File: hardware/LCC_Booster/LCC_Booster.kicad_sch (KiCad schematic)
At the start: 9 parts, among them J1 A00-216-262-450, J2 Barrel_Jack_MountingPin, J3 Screw_Terminal_01x08, J4 Screw_Terminal_01x02, J5 Screw_Terminal_01x02, SW1 SW_Push, SW2 SW_Slide_DPDT, U1 ACPL-214-500E

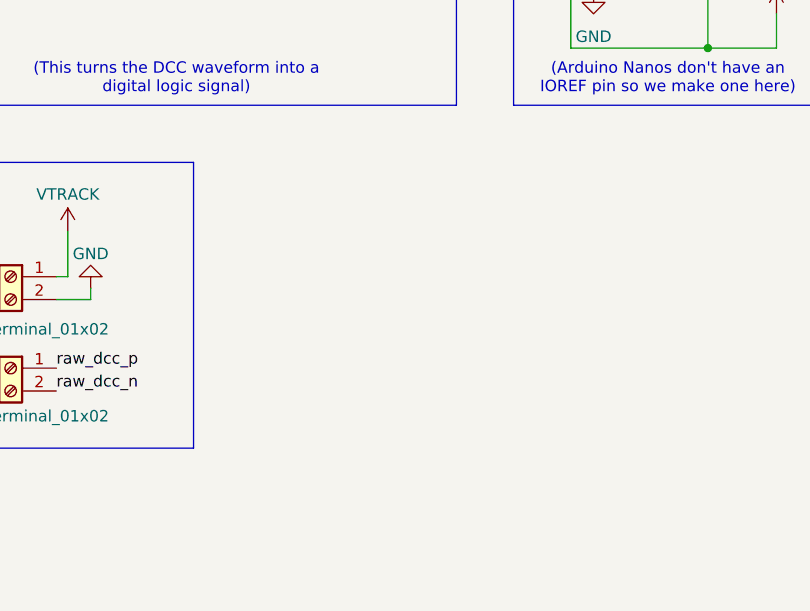
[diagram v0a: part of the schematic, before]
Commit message: Shrunk and added standoffs
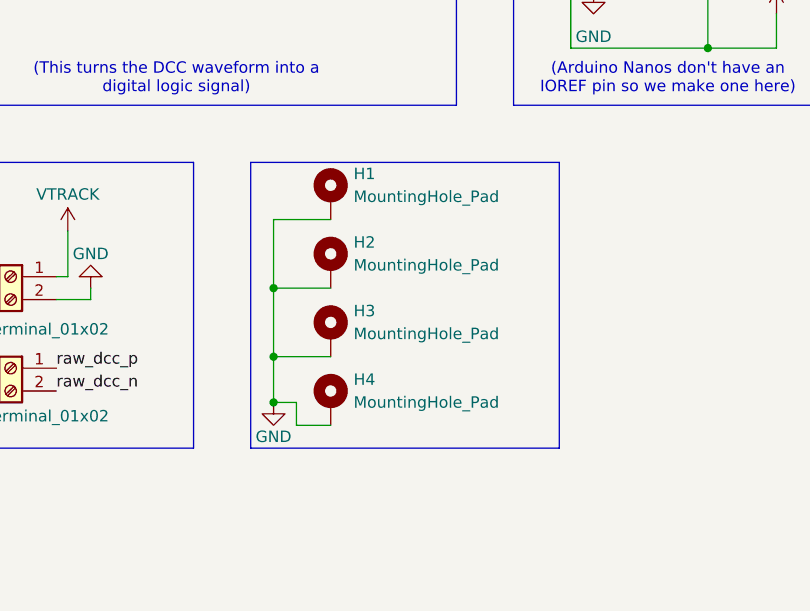
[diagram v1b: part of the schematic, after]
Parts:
- added H1, H2, H3, H4: MountingHole_Pad, MountingHole:MountingHole_4.3mm_M4_Pad_Via, symbol Mechanical:MountingHole_Pad
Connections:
- net GND: now also H1.1, H2.1, H3.1, H4.1

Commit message: Fixed some footprints
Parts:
- removed J2: Barrel_Jack_MountingPin, Connector_BarrelJack:BarrelJack_CUI_PJ-063AH_Horizontal, symbol Connector:Barrel_Jack_MountingPin
- added J2: 54-00166, 54-00166:TENSILITY_54-00166, symbol 54-00166:54-00166
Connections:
- net GND: now also J2.B, J2.C
- net VIN: now also J2.A
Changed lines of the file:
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@@
 	(paper "A4")
 	(junction
+		(at 99.06 137.16)
+		(diameter 0)
+		(color 0 0 0 0)
+	)
+	(junction
 		(at 198.12 66.04)
 		(diameter 0)
@@
 	)
 	(junction
-		(at 93.98 143.51)
-		(diameter 0)
-		(color 0 0 0 0)
-	)
-	(junction
 		(at 198.12 73.66)
 		(diameter 0)
@@
 	(wire
 		(pts
+			(xy 99.06 134.62) (xy 99.06 137.16)
+		)
+		(stroke
+			(width 0)
+			(type default)
+		)
+	)
+	(wire
+		(pts
 			(xy 125.73 19.05) (xy 125.73 48.26)
 		)
@@
 	(wire
 		(pts
-			(xy 93.98 143.51) (xy 90.17 143.51)
-		)
-		(stroke
-			(width 0)
-			(type default)
-		)
-	)
-	(wire
-		(pts
 			(xy 83.82 48.26) (xy 85.09 48.26)
 		)
@@
 	(wire
 		(pts
+			(xy 97.79 134.62) (xy 99.06 134.62)
+		)
+		(stroke
+			(width 0)
+			(type default)
+		)
+	)
+	(wire
+		(pts
 			(xy 93.98 144.78) (xy 93.98 143.51)
 		)
@@
 	(wire
 		(pts
-			(xy 90.17 143.51) (xy 90.17 142.24)
-		)
-		(stroke
-			(width 0)
-			(type default)
-		)
-	)
-	(wire
-		(pts
 			(xy 45.72 20.32) (xy 43.18 20.32)
 		)
@@
 	)
 	(symbol
+		(lib_id "54-00166:54-00166")
+		(at 92.71 134.62 0)
+		(unit 1)
+		(exclude_from_sim no)
+		(in_bom yes)
+		(on_board yes)
+		(dnp no)
+		(fields_autoplaced yes)
+		(property "Reference" "J2"
+			(at 87.9503 125.73 0)
+			(effects
+				(font
+					(size 1.27 1.27)
+				)
+			)
+		)
+		(property "Value" "54-00166"
+			(at 87.9503 128.27 0)
+			(effects
+				(font
+					(size 1.27 1.27)
+				)
+			)
+		)
+		(property "Footprint" "54-00166:TENSILITY_54-00166"
+			(at 92.71 134.62 0)
+			(effects
+				(font
+					(size 1.27 1.27)
+				)
+				(justify bottom)
+				(hide yes)
+			)
+		)
+		(property "Datasheet" ""
+			(at 92.71 134.62 0)
+			(effects
+				(font
+					(size 1.27 1.27)
+				)
+				(hide yes)
+			)
+		)
+		(property "Description" ""
+			(at 92.71 134.62 0)
+			(effects
+				(font
+					(size 1.27 1.27)
+				)
+				(hide yes)
+			)
+		)
+		(property "PARTREV" "A"
+			(at 92.71 134.62 0)
+			(effects
+				(font
+					(size 1.27 1.27)
+				)
+				(justify bottom)
+				(hide yes)
+			)
+		)
+		(property "STANDARD" "Manufacturer Recommendations"
+			(at 92.71 134.62 0)
+			(effects
+				(font
+					(size 1.27 1.27)
+				)
+				(justify bottom)
+				(hide yes)
+			)
+		)
+		(property "SNAPEDA_PN" "54-00166"
+			(at 92.71 134.62 0)
+			(effects
+				(font
+					(size 1.27 1.27)
+				)
+				(justify bottom)
+				(hide yes)
+			)
+		)
+		(property "MAXIMUM_PACKAGE_HEIGHT" "11.2mm"
+			(at 92.71 134.62 0)
+			(effects
+				(font
+					(size 1.27 1.27)
+				)
+				(justify bottom)
+				(hide yes)
+			)
+		)
+		(property "MANUFACTURER" "TENSILITY"
+			(at 92.71 134.62 0)
+			(effects
+				(font
+					(size 1.27 1.27)
+				)
+				(justify bottom)
+				(hide yes)
+			)
+		)
+		(pin "C"
+		)
+		(pin "B"
+		)
+		(pin "A"
+		)
+		(instances
+			(project "LCC_Booster"
+				(path "/e8524381-bb01-4107-93ec-8133e878a3da"
+					(reference "J2")
+					(unit 1)
+				)
+			)
+		)
+	)
+	(symbol
 		(lib_id "Connector:Screw_Terminal_01x02")
 		(at 168.91 74.93 0)
@@
 					(unit 1)
 				)
-			)
-		)
-	)
-	(symbol
-		(lib_id "Connector:Barrel_Jack_MountingPin")
-		(at 90.17 134.62 0)
-		(unit 1)
-		(exclude_from_sim no)
-		(in_bom yes)
-		(on_board yes)
-		(dnp no)
-		(property "Reference" "J2"
-			(at 90.17 129.032 0)
-			(effects
-				(font
-					(size 1.27 1.27)
-				)
-			)
-		)
-		(property "Value" "Barrel_Jack_MountingPin"
-			(at 83.312 139.954 90)
-			(effects
-				(font
-					(size 1.27 1.27)
-				)
-			)
-		)
-		(property "Footprint" "Connector_BarrelJack:BarrelJack_CUI_PJ-063AH_Horizontal"
-			(at 91.44 135.636 0)
-			(effects
-				(font
-					(size 1.27 1.27)
-				)
-				(hide yes)
-			)
-		)
-		(property "Datasheet" "~"
-			(at 91.44 135.636 0)
-			(effects
-				(font
-					(size 1.27 1.27)
-				)
-				(hide yes)
-			)
-		)
-		(property "Description" "DC Barrel Jack with a mounting pin"
-			(at 90.17 134.62 0)
-			(effects
-				(font
-					(size 1.27 1.27)
-				)
-				(hide yes)
-			)
-		)
-		(pin "2"
-		)
-		(pin "MP"
-		)
-		(pin "1"
-		)
-		(instances
-			(project "LCC_Booster"
-				(path "/e8524381-bb01-4107-93ec-8133e878a3da"
-					(reference "J2")
-					(unit 1)
-				)

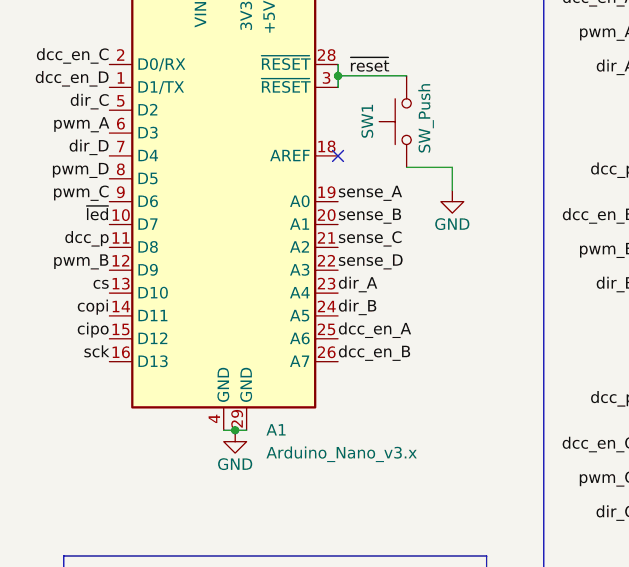
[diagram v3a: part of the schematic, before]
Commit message: LCC Command Station Shield
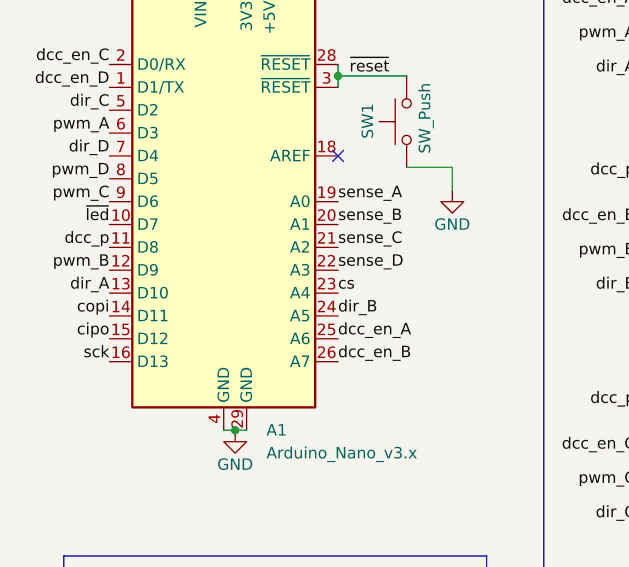
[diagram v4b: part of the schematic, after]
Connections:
- net cs: now also A1.23 (A4); no longer A1.13 (D10)
- net dir_A: now also A1.13 (D10); no longer A1.23 (A4)
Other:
- company: (none) -> TMRC
- title: (none) -> Arduino Nano LCC Booster
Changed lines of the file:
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@@
 	(generator_version "8.0")
 	(paper "A4")
+	(title_block
+		(title "Arduino Nano LCC Booster")
+		(date "2024-04-28")
+		(rev "1.0")
+		(company "TMRC")
+		(comment 1 "Noah Paladino")
+	)
 	(junction
 		(at 99.06 137.16)
@@
 		)
 	)
+	(label "cs"
+		(at 50.8 55.88 0)
+		(fields_autoplaced yes)
+		(effects
+			(font
+				(size 1.27 1.27)
+			)
+			(justify left bottom)
+		)
+	)
 	(label "pwr_n"
 		(at 53.34 124.46 0)
@@
 		)
 	)
-	(label "dir_A"
-		(at 50.8 55.88 0)
-		(fields_autoplaced yes)
-		(effects
-			(font
-				(size 1.27 1.27)
-			)
-			(justify left bottom)
-		)
-	)
 	(label "dcc_p"
 		(at 83.82 68.58 180)
@@
 		)
 	)
+	(label "dir_A"
+		(at 25.4 55.88 180)
+		(fields_autoplaced yes)
+		(effects
+			(font
+				(size 1.27 1.27)
+			)
+			(justify right bottom)
+		)
+	)
 	(label "out1_D"
 		(at 109.22 93.98 0)
@@
 		(fields_autoplaced yes)
 		(effects
-			(font
-				(size 1.27 1.27)
-			)
-			(justify right bottom)
-		)
-	)
-	(label "cs"
-		(at 25.4 55.88 180)
-		(fields_autoplaced yes)
-		(effects

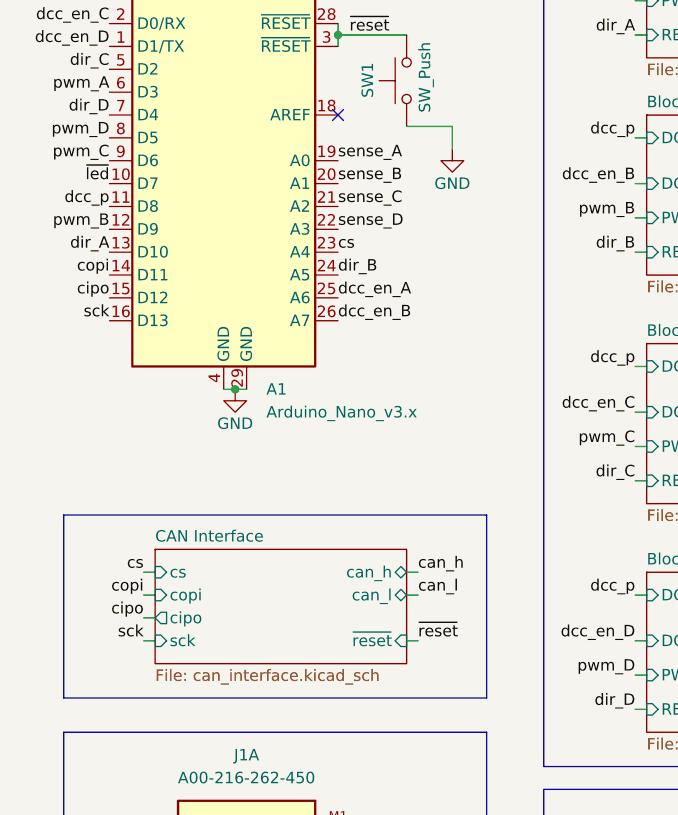
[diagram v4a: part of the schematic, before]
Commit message: Start to work on code structure and added MCP2515 interrupt
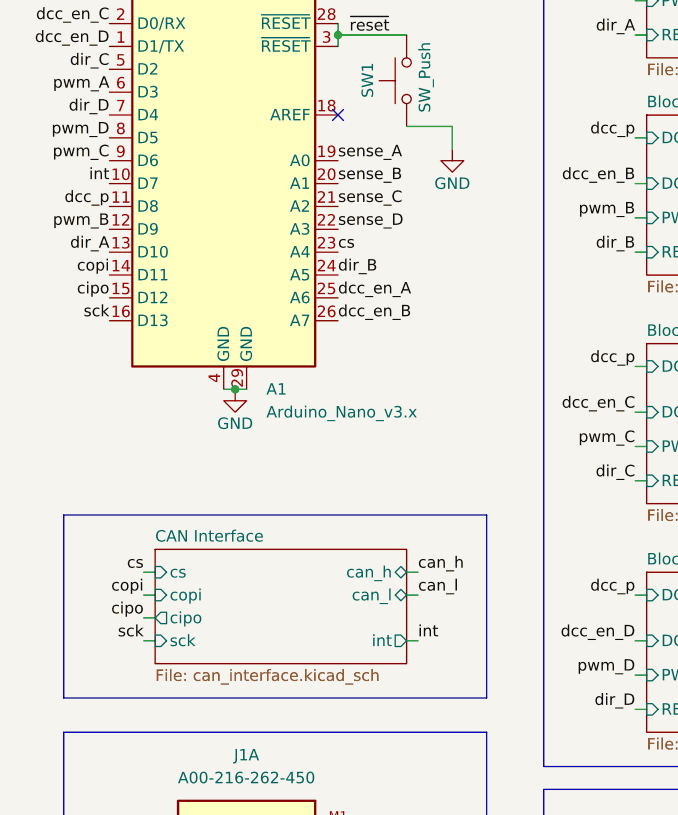
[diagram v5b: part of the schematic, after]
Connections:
- net ~{led} renamed int
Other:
- sheet CAN Interface ports: added int; removed ~{reset}
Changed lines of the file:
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@@
 	(wire
 		(pts
-			(xy 58.42 99.06) (xy 59.69 99.06)
-		)
-		(stroke
-			(width 0)
-			(type default)
-		)
-	)
-	(wire
-		(pts
 			(xy 125.73 48.26) (xy 137.16 48.26)
 		)
@@
 	(wire
 		(pts
+			(xy 58.42 99.06) (xy 59.69 99.06)
+		)
+		(stroke
+			(width 0)
+			(type default)
+		)
+	)
+	(wire
+		(pts
 			(xy 231.14 22.86) (xy 234.95 22.86)
 		)
@@
 		)
 	)
+	(label "int"
+		(at 59.69 99.06 0)
+		(fields_autoplaced yes)
+		(effects
+			(font
+				(size 1.27 1.27)
+			)
+			(justify left bottom)
+		)
+	)
 	(label "out1_A"
 		(at 109.22 19.05 0)
@@
 		)
 	)
-	(label "~{led}"
+	(label "int"
 		(at 25.4 48.26 180)
 		(fields_autoplaced yes)
@@
 		)
 	)
-	(label "~{reset}"
-		(at 59.69 99.06 0)
-		(fields_autoplaced yes)
-		(effects
-			(font
-				(size 1.27 1.27)
-			)
-			(justify left bottom)
-		)
-	)
 	(label "can_gnd"
 		(at 53.34 134.62 0)
@@
 			)
 		)
-		(pin "~{reset}" input
+		(pin "int" output
 			(at 58.42 99.06 0)
 			(effects

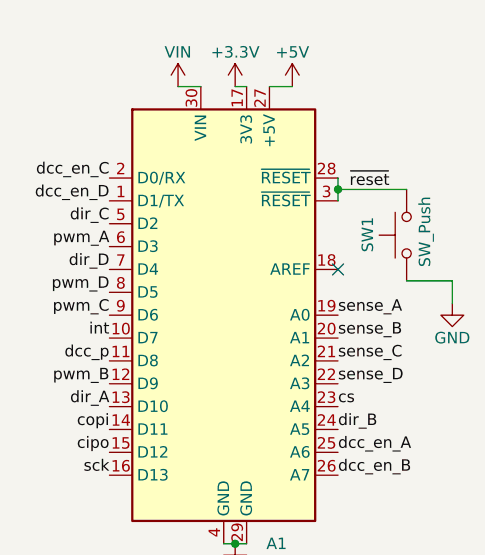
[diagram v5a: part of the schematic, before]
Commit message: Added MCP2515 Interrupt capability
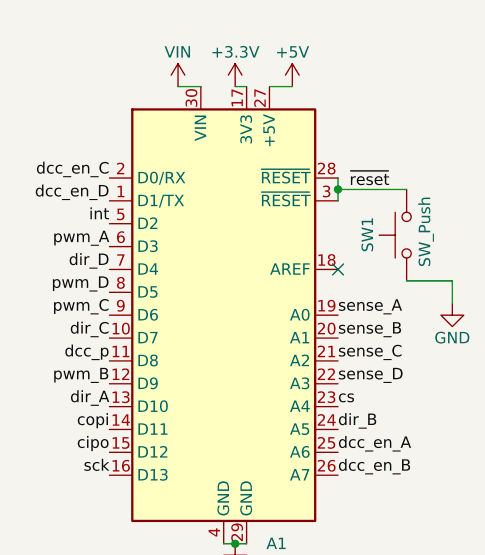
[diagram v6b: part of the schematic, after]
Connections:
- net dir_C: now also A1.10 (D7); no longer A1.5 (D2)
- net int: now also A1.5 (D2); no longer A1.10 (D7)
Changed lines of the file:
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@@
-		)
-	)
-	(label "dir_C"
-		(at 25.4 35.56 180)
-		(fields_autoplaced yes)
-		(effects
-			(font
-				(size 1.27 1.27)
-			)
-			(justify right bottom)
 		)
 	)
@@
 		)
 	)
+	(label "int"
+		(at 25.4 35.56 180)
+		(fields_autoplaced yes)
+		(effects
+			(font
+				(size 1.27 1.27)
+			)
+			(justify right bottom)
+		)
+	)
 	(label "out1_C"
 		(at 109.22 68.58 0)
@@
 		)
 	)
+	(label "dir_C"
+		(at 25.4 48.26 180)
+		(fields_autoplaced yes)
+		(effects
+			(font
+				(size 1.27 1.27)
+			)
+			(justify right bottom)
+		)
+	)
 	(label "dir_B"
 		(at 50.8 58.42 0)
@@
 		)
 	)
-	(label "int"
-		(at 25.4 48.26 180)
-		(fields_autoplaced yes)
-		(effects
-			(font
-				(size 1.27 1.27)
-			)
-			(justify right bottom)
-		)
-	)

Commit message: Better Solder Jumpers, Better Pizza
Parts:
- removed SW2: SW_Slide_DPDT, Button_Switch_THT:SW_CK_JS202011CQN_DPDT_Straight, symbol Switch:SW_Slide_DPDT
- added JP1, JP2: SolderJumper_3_Bridged12, Jumper:SolderJumper-3_P1.3mm_Bridged12_RoundedPad1.0x1.5mm_NumberLabels, symbol Jumper:SolderJumper_3_Bridged12
- added JP5: SolderJumper_2_Open, Jumper:SolderJumper-2_P1.3mm_Open_RoundedPad1.0x1.5mm, symbol Jumper:SolderJumper_2_Open
- J5: now not fitted
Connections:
- net cs is gone; now on net dir_B: A1.23 (A4)
- net +3.3V: now also JP2.1 (A)
- net +5V: now also JP1.1 (A), JP2.3 (B)
- net 3v3_IOREF: now also JP1.2 (C)
- net GND: now also JP1.3 (B), JP5.2 (B)
- net IOREF: now also JP2.2 (C)
- net can_shield: now also JP5.1 (A)
- net dir_A: now also A1.24 (A5); no longer A1.13 (D10)
- net dir_B: no longer A1.24 (A5)
- net int renamed int_cantx
- new net cs_canrx: A1.13 (D10)
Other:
- sheet CAN Interface ports: added cs_canrx, int_cantx; removed cs, int

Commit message: Update to hardware v2 and cleanup
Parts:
- removed J4, J5: Screw_Terminal_01x02, TerminalBlock_Phoenix:TerminalBlock_Phoenix_MKDS-1,5-2_1x02_P5.00mm_Horizontal, symbol Connector:Screw_Terminal_01x02
- removed JP1, JP2: SolderJumper_3_Bridged12, Jumper:SolderJumper-3_P1.3mm_Bridged12_RoundedPad1.0x1.5mm_NumberLabels, symbol Jumper:SolderJumper_3_Bridged12
- added C34, C35: C100n, Capacitor_SMD:C_0402_1005Metric_Pad0.74x0.62mm_HandSolder, symbol Device:C
- added JP2: SolderJumper_2_Open, Jumper:SolderJumper-2_P1.3mm_Bridged_RoundedPad1.0x1.5mm, symbol Jumper:SolderJumper_2_Bridged
- added JP3: SolderJumper_2_Open, Jumper:SolderJumper-2_P1.3mm_Open_RoundedPad1.0x1.5mm, symbol Jumper:SolderJumper_2_Open
- added U2: ACPL-214-500E, Package_SO:SOP-4_4.4x2.6mm_P1.27mm, symbol Isolator:ACPL-214-500E
- J3: footprint TerminalBlock_Phoenix:TerminalBlock_Phoenix_MKDS-1,5-8_1x08_P5.00mm_Horizontal -> TerminalBlock_Phoenix:TerminalBlock_Phoenix_MKDS-1,5-12_1x12_P5.00mm_Horizontal; symbol Connector:Screw_Terminal_01x08 -> Connector:Screw_Terminal_01x12
- renumbered JP5 to JP1
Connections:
- net +3.3V: now also JP2.1 (A)
- net +5V: now also JP3.2 (B)
- net GND: now also J3.11 (Pin_11), C34.2, C35.2, U2.2
- net IOREF: now also C34.1, C35.1, JP2.2 (B), JP3.1 (A), U2.4
- net VTRACK: now also J3.12 (Pin_12)
- net dcc_en_A: now also A1.26 (A7); no longer A1.25 (A6)
- net dcc_en_B: now also A1.25 (A6); no longer A1.26 (A7)
- net dcc_en_C: now also A1.1 (D1/TX); no longer A1.2 (D0/RX)
- net dcc_en_D: now also A1.2 (D0/RX); no longer A1.1 (D1/TX)
- net out1_A: now also J3.10 (Pin_10); no longer J3.8 (Pin_8)
- net out1_B: now also J3.8 (Pin_8); no longer J3.6 (Pin_6)
- net out1_C: now also J3.6 (Pin_6); no longer J3.4 (Pin_4)
- net out1_D: now also J3.4 (Pin_4); no longer J3.2 (Pin_2)
- net out2_A: now also J3.9 (Pin_9); no longer J3.7 (Pin_7)
- net out2_B: now also J3.7 (Pin_7); no longer J3.5 (Pin_5)
- net out2_C: now also J3.5 (Pin_5); no longer J3.3 (Pin_3)
- net out2_D: now also J3.3 (Pin_3); no longer J3.1 (Pin_1)
- net pwm_A: now also A1.12 (D9); no longer A1.6 (D3)
- net pwm_B: now also A1.9 (D6); no longer A1.12 (D9)
- net pwm_C: now also A1.8 (D5); no longer A1.9 (D6)
- net pwm_D: now also A1.6 (D3); no longer A1.8 (D5)
- net raw_dcc_n: now also J3.1 (Pin_1), U2.1
- net raw_dcc_p: now also J3.2 (Pin_2)
- net sense_A: now also A1.22 (A3); no longer A1.19 (A0)
- net sense_B: now also A1.21 (A2); no longer A1.20 (A1)
- net sense_C: now also A1.20 (A1); no longer A1.21 (A2)
- net sense_D: now also A1.19 (A0); no longer A1.22 (A3)
- new net dcc_n: U2.3
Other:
- sheet Block Driver A ports: added DCC_n; removed none
- sheet Block Driver B ports: added DCC_n; removed none
- sheet Block Driver C ports: added DCC_n; removed none
- sheet Block Driver D ports: added DCC_n; removed none
